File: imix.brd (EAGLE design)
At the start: 87 x 102.5 mm, 149 parts, among them Q2 AO3415, Q3 AO3415, Q4 AO3415, Q5 AO3415, U1 BQ2423X, U10 ISL29035, U11 FX0S8700CQ, U12 296-12686-1-ND, U3 TLV3202, U4 LM358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

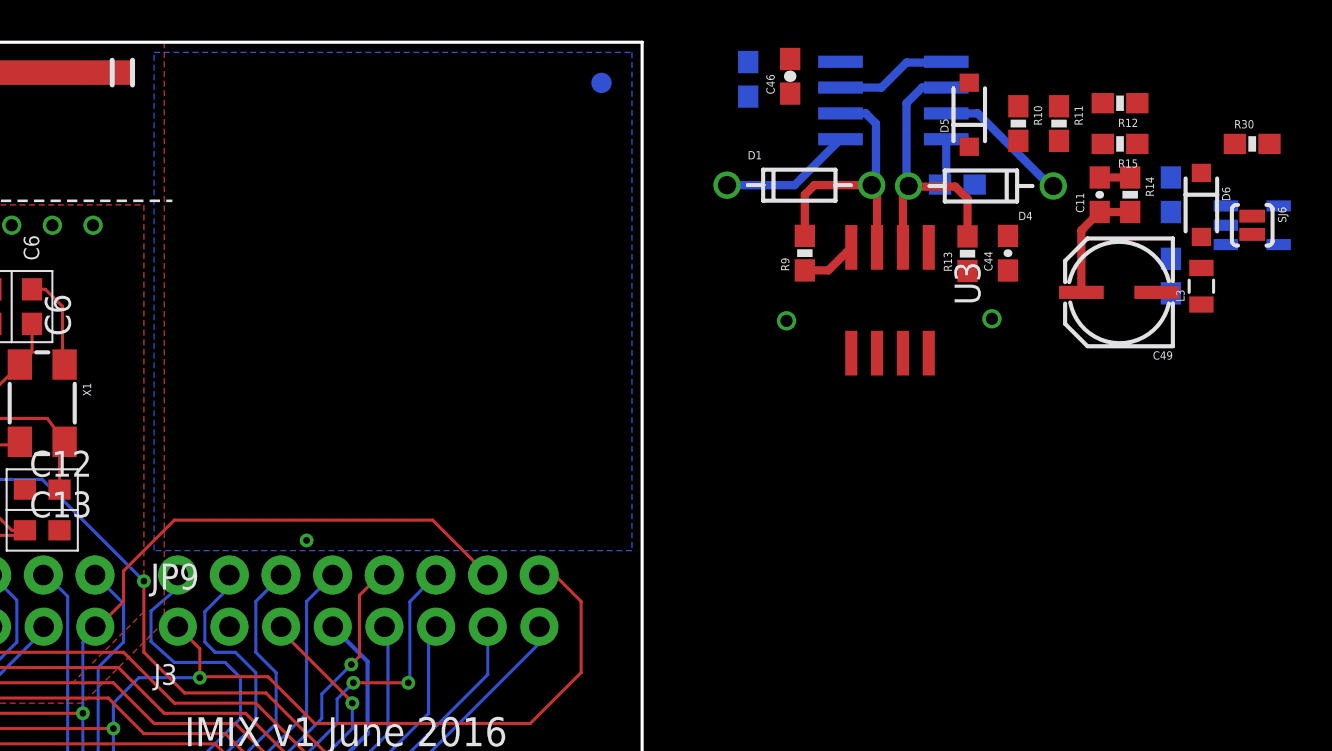
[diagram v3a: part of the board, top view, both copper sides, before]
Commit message: Rearranged RNG
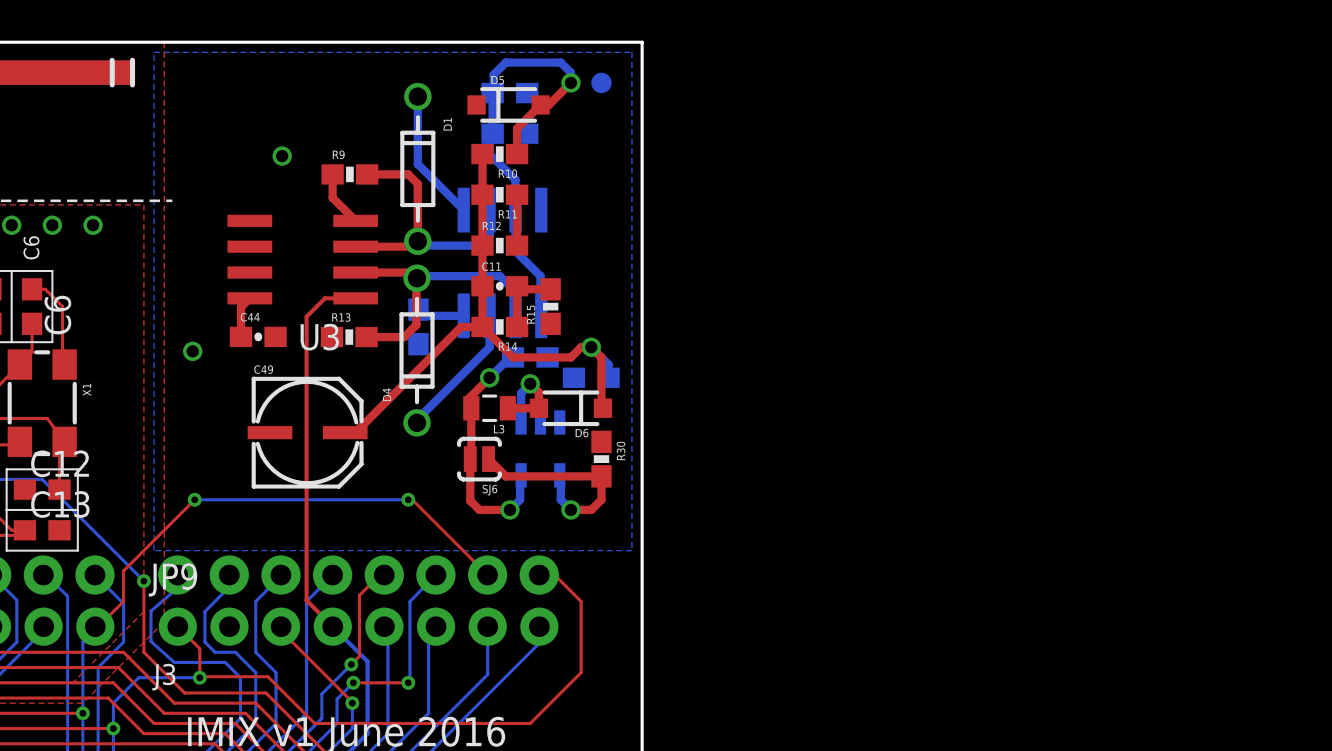
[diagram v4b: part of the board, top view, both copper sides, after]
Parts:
- moved C49 40.5 mm to (70.5, 67.0), turned to 0 degrees
- moved SJ6 39.7 mm to (79.0, 65.5), turned to 180 degrees
- moved C44 37.1 mm to (68.1, 71.5), turned to 0 degrees
- moved U12 36.7 mm to (82.0, 66.0), turned to 180 degrees
- moved R30 35.6 mm to (85.0, 65.5), turned to 270 degrees
- moved L3 35.5 mm to (79.5, 68.0), turned to 180 degrees
- moved D6 32.6 mm to (83.5, 68.0), turned to 180 degrees
- moved C48 31.8 mm to (81.5, 70.5), turned to 180 degrees
- moved R14 31.7 mm to (80.0, 72.0), turned to 180 degrees
- moved R12 31.3 mm to (80.0, 76.0), turned to 0 degrees
- moved R13 30.7 mm to (72.6, 71.5), turned to 0 degrees
- moved C47 29.9 mm to (84.5, 69.5), turned to 0 degrees
- moved C11 29.8 mm to (80.0, 74.0), turned to 0 degrees
- moved R15 29.1 mm to (82.5, 73.0), turned to 90 degrees
- moved U3 28.9 mm to (70.3, 75.3), turned to 90 degrees
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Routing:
- net VHIGH: track 8.18 -> 31.0 mm, vias 0 -> 1
- net TRNG_OUT: track 22.0 -> 40.6 mm, vias 2 -> 1
- net N$66: track 5.73 -> 22.6 mm, vias 0 -> 1
- net VCC_TRNG_3V3: track 77.5 -> 91.7 mm, vias 1 -> 3
- net TRNG_EN: track 22.2 -> 32.9 mm, vias 1 -> 2
- net N$43: track 0.00 -> 4.99 mm, vias 0 -> 1
- net VHIGHSAMPLE: track 0.00 -> 2.50 mm
- net N$46: track 1.50 -> 3.71 mm
- net USART3_TX: track 96.3 -> 97.1 mm, vias 4 -> 6

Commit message: DFM is almost passing
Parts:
- added F10, F7, F8, F9: FIDUCIAL, GeekAmmo:FIDUCIAL
- moved R12 4.53 mm to (83.0, 79.4), turned to 270 degrees
- moved R14 4.20 mm to (80.0, 76.2)
- moved C49 2.56 mm to (72.1, 65.0), turned to 90 degrees
- moved R15 1.80 mm to (83.1, 74.7), turned to 270 degrees
- moved R16 1.00 mm to (9.00, 54.5)
- moved C14 0.50 mm to (12.5, 52.0)
- moved U12 0.50 mm to (82.0, 65.5)
- moved R11 0.10 mm to (80.0, 78.4)
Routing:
- net GND: track 158.5 -> 191.8 mm, vias 82 -> 85
- net VCC_TRNG_3V3: track 91.7 -> 116.7 mm, vias 3 -> 5
- net TRNG_EN: track 32.9 -> 46.4 mm
- net N$46: track 3.71 -> 12.0 mm, vias 0 -> 1
- net VCC_NRF_3V3: track 54.0 -> 47.1 mm
- net VHIGH: track 31.0 -> 35.0 mm, vias 1 -> 2
- net N$53: track 6.40 -> 8.09 mm
- net TWI2_SCL: track 127.5 -> 126.9 mm
- net VCC_IN: track 84.1 -> 83.6 mm
- net N$43: track 4.99 -> 5.49 mm
- removed copper zone on layer 15, net VCC_TRNG_3V3
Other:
- board text added: "( indicates fiducial)"
- board text added: "Cut to measure power"
- board text added: "F10"
- board text added: "F7"
- board text added: "F8"
- board text added: "F9"
- board text added: "Mitered inner corners"
- board text added: "R11"
- board text added: "R12"
- board text added: "SJ6"
- board text added: "True RNG Ben Lampert June 2016"
- board text added: "USB1"
- board text added: "USB2"
- board text removed: "DBG USB"
- board text removed: "Q1"
- board text removed: "TARGET USB"
